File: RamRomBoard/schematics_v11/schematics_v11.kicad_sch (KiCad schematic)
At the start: 84 parts, among them J10 Micro_SD_Card_Det2, J3 VSEL, J5 Screw_Terminal_01x02, J6 USB_B_Micro, J7 STM32F401, J8 Dual LED Socket, J9 JTAG, SW1 033TBVSA, SW2 SW_Push, U1 74LVC125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

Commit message: first boards done, start of coding
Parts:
- added H5: Logo kicad, Symbol:KiCad-Logo2_6mm_SilkScreen, symbol Mechanical:MountingHole
- added H6: Logo Open Source Hardware, Symbol:OSHW-Logo2_7.3x6mm_SilkScreen, symbol Mechanical:MountingHole
- added H7: Logo 100%, my_own:Logo_100ProzentOffner_10x2.7mm, symbol Mechanical:MountingHole
- added JP1: CTRL, Jumper:SolderJumper-2_P1.3mm_Open_RoundedPad1.0x1.5mm, symbol Jumper:SolderJumper_2_Open
- added TP15: ., Connector_PinHeader_1.00mm:PinHeader_1x01_P1.00mm_Vertical, symbol Connector:TestPoint
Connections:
- net +3V3: no longer R5.1, R6.1
- net GND: now also R5.2, R6.2
- net at TP8.1, U4.5 (CTRL0): now also R5.1, JP1.1 (A); no longer R5.2
- net CNT renamed CPC
- net CTRL1: no longer names the net of TP9.1, U4.6 (CTRL1)
- net CTRL1: now also R6.1, JP1.2 (B); no longer J7.16 (Pin_16), R6.2
- net ~{CEDAT_EN} renamed ~{CERAMWR}
- net ~{MRAM_WR} renamed ~{MRAMWR}
- new net CTRL: J7.16 (Pin_16), TP15.1
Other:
- note added: "Graphics"
- note added: "~{MRAMWR} is Write Pulse from STM32."
- note removed: "~{MRAM_WR} is Write Pulse from STM32."
- moved on the sheet: R3, R4, R5, R6, TP8, TP9, U4

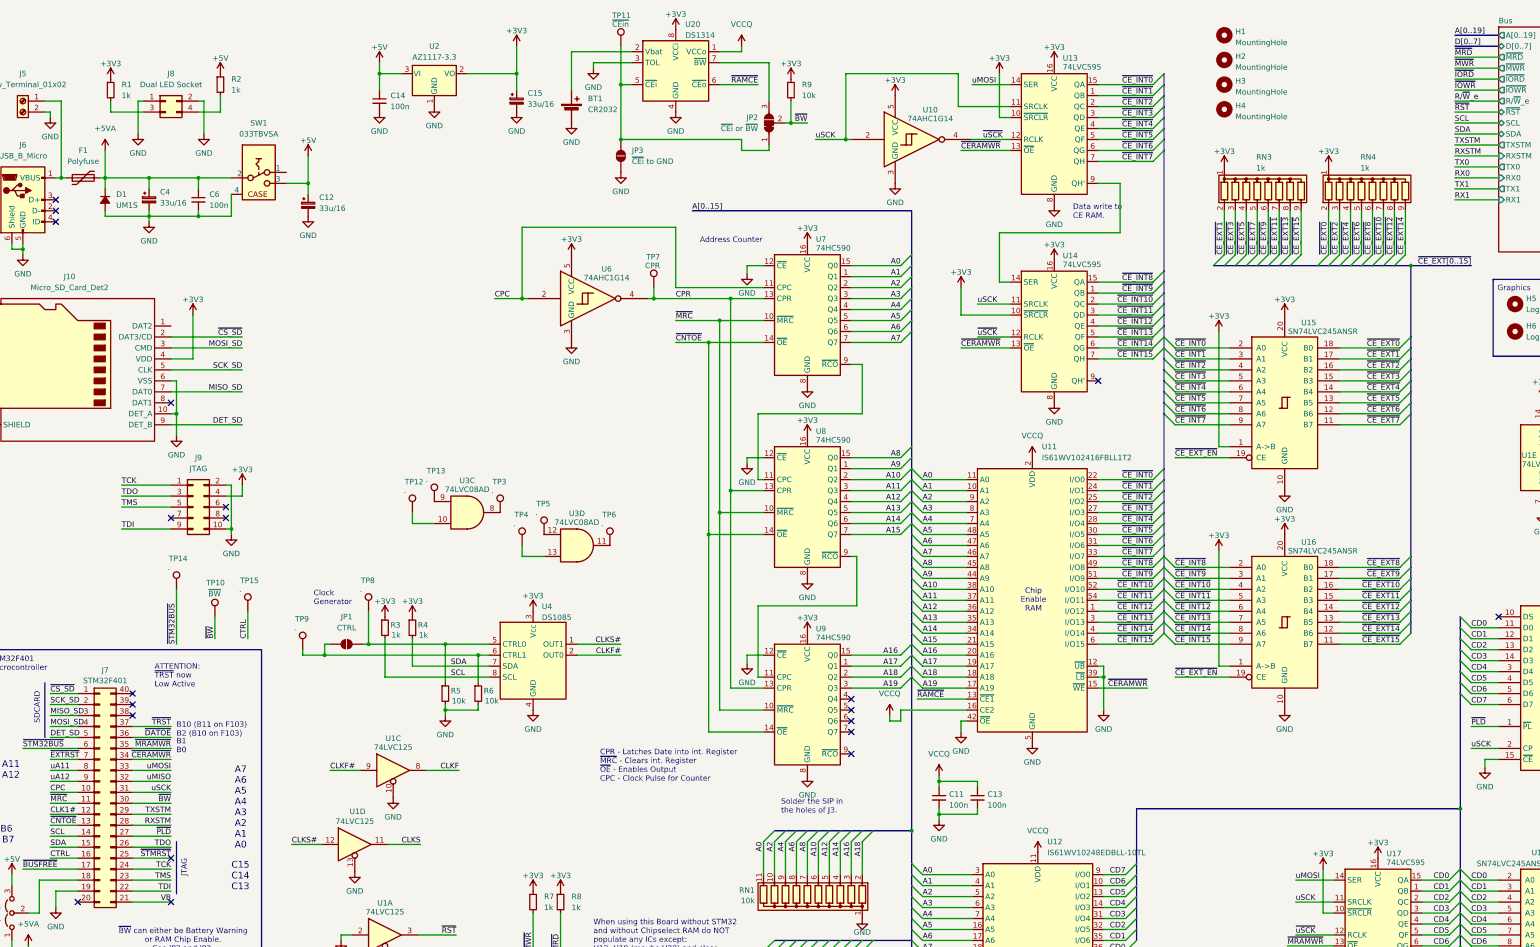
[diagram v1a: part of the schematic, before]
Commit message: new vhdl code
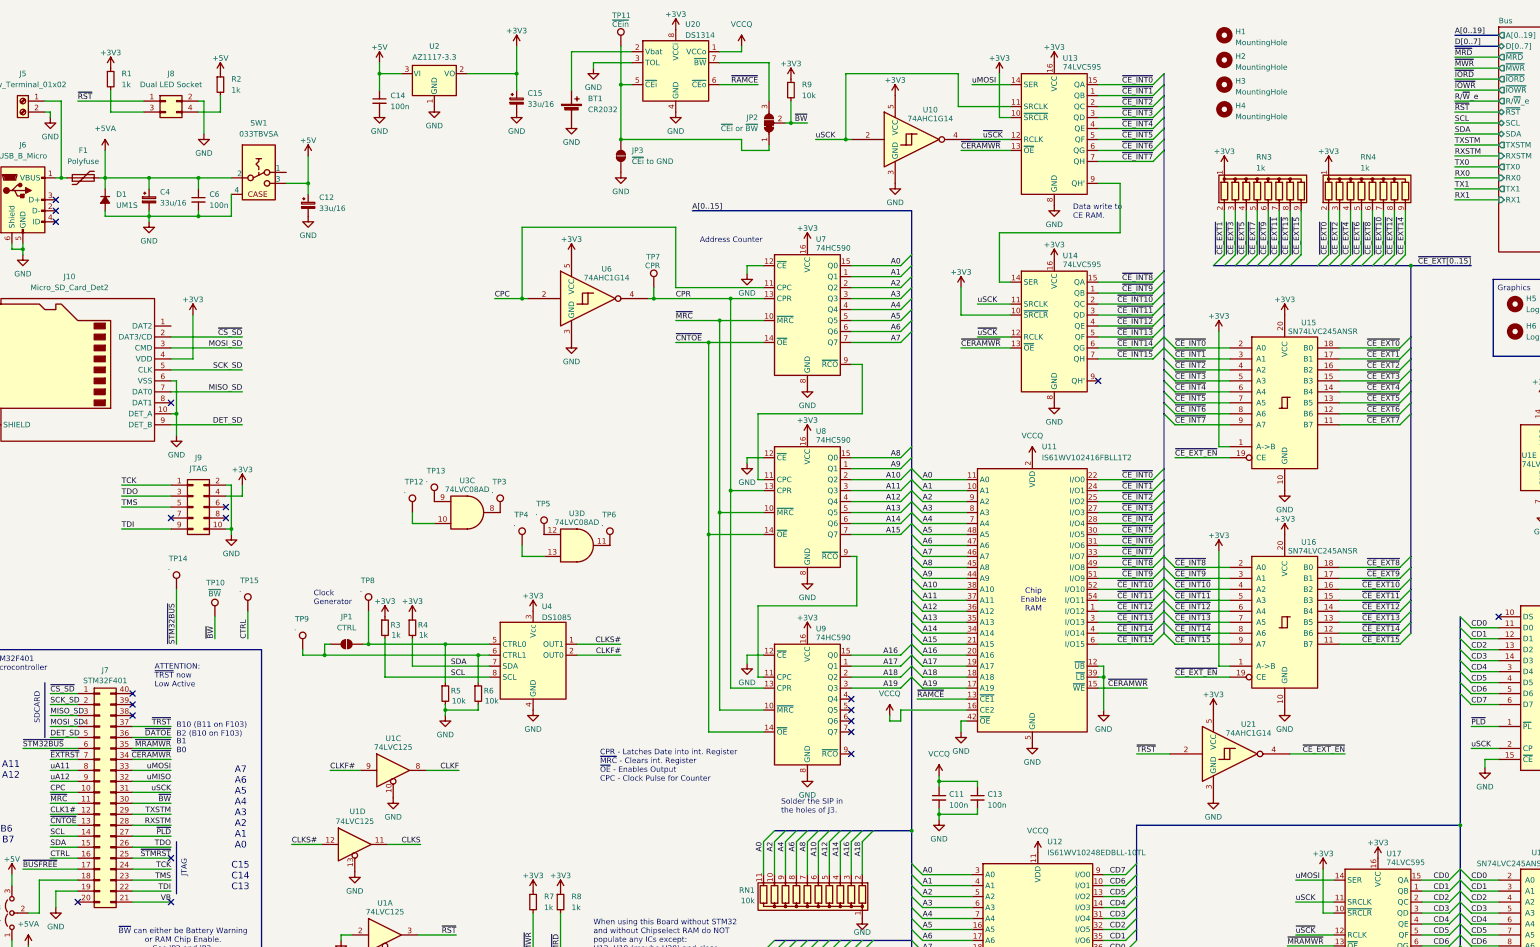
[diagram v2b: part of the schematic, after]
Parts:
- added U21: 74AHC1G14, Package_TO_SOT_SMD:SOT-23-5, symbol 74xGxx:74AHC1G14
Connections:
- net +3V3: now also U21.5 (VCC)
- net GND: now also U21.3 (GND); no longer J8.1 (Pin_1)
- net ~{CE_EXT_EN}: now also U21.4
- net ~{RST}: now also J8.1 (Pin_1)
- net ~{TRST}: now also U21.2
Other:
- moved on the sheet: R1

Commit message: graphic updates
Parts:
- added R11: 1k, Resistor_SMD:R_1206_3216Metric, symbol Device:R_Small
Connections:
- net +3V3: now also R11.1
- net R/~{W}_e: now also R11.2
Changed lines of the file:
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@@
 		(company "100% Offner")
 		(comment 1 "v1.0: Initial")
-		(comment 2 "v1.1: CTRL0 and CTRL1 ch. to Pulldown, second LED shows ~{RST}, U21 new")
+		(comment 2 "v1.1: CTRL0 and CTRL1 ch. to Pulldown, second LED shows ~{RST}, U21 new, R/W Pullup")
 	)
 	(junction
@@
 	(wire
 		(pts
+			(xy 137.16 220.98) (xy 137.16 229.87)
+		)
+		(stroke
+			(width 0)
+			(type default)
+		)
+	)
+	(wire
+		(pts
 			(xy 275.59 222.25) (xy 280.67 222.25)
 		)
@@
 		)
 	)
+	(label "R{slash}~{W}_e"
+		(at 137.16 229.87 90)
+		(fields_autoplaced yes)
+		(effects
+			(font
+				(size 1.27 1.27)
+			)
+			(justify left bottom)
+		)
+	)
 	(label "A12"
 		(at 212.09 204.47 270)
@@
 	(symbol
 		(lib_id "power:+3V3")
+		(at 137.16 215.9 0)
+		(unit 1)
+		(exclude_from_sim no)
+		(in_bom yes)
+		(on_board yes)
+		(dnp no)
+		(fields_autoplaced yes)
+		(property "Reference" "#PWR0133"
+			(at 137.16 219.71 0)
+			(effects
+				(font
+					(size 1.27 1.27)
+				)
+				(hide yes)
+			)
+		)
+		(property "Value" "+3V3"
+			(at 137.16 212.3242 0)
+			(effects
+				(font
+					(size 1.27 1.27)
+				)
+			)
+		)
+		(property "Footprint" ""
+			(at 137.16 215.9 0)
+			(effects
+				(font
+					(size 1.27 1.27)
+				)
+				(hide yes)
+			)
+		)
+		(property "Datasheet" ""
+			(at 137.16 215.9 0)
+			(effects
+				(font
+					(size 1.27 1.27)
+				)
+				(hide yes)
+			)
+		)
+		(property "Description" "Power symbol creates a global label with name \"+3V3\""
+			(at 137.16 215.9 0)
+			(effects
+				(font
+					(size 1.27 1.27)
+				)
+				(hide yes)
+			)
+		)
+		(pin "1"
+		)
+		(instances
+			(project "schematics_v11"
+				(path "/2eaa3998-c9cb-43b1-9b23-df656c8158b0"
+					(reference "#PWR0133")
+					(unit 1)
+				)
+			)
+		)
+	)
+	(symbol
+		(lib_id "power:+3V3")
 		(at 109.22 152.4 0)
 		(unit 1)
@@
 	)
 	(symbol
+		(lib_id "Device:R_Small")
+		(at 137.16 218.44 0)
+		(unit 1)
+		(exclude_from_sim no)
+		(in_bom yes)
+		(on_board yes)
+		(dnp no)
+		(property "Reference" "R11"
+			(at 138.43 217.805 0)
+			(effects
+				(font
+					(size 1.27 1.27)
+				)
+				(justify left)
+			)
+		)
+		(property "Value" "1k"
+			(at 138.6586 220.1422 0)
+			(effects
+				(font
+					(size 1.27 1.27)
+				)
+				(justify left)
+			)
+		)
+		(property "Footprint" "Resistor_SMD:R_1206_3216Metric"
+			(at 137.16 218.44 0)
+			(effects
+				(font
+					(size 1.27 1.27)
+				)
+				(hide yes)
+			)
+		)
+		(property "Datasheet" "~"
+			(at 137.16 218.44 0)
+			(effects
+				(font
+					(size 1.27 1.27)
+				)
+				(hide yes)
+			)
+		)
+		(property "Description" "Resistor, small symbol"
+			(at 137.16 218.44 0)
+			(effects
+				(font
+					(size 1.27 1.27)
+				)
+				(hide yes)
+			)
+		)
+		(pin "1"
+		)
+		(pin "2"
+		)
+		(instances
+			(project "schematics_v11"
+				(path "/2eaa3998-c9cb-43b1-9b23-df656c8158b0"
+					(reference "R11")
+					(unit 1)
+				)
+			)
+		)
+	)
+	(symbol
 		(lib_id "Mechanical:MountingHole")
 		(at 303.53 17.78 0)
@@
 	(symbol
 		(lib_id "Graphic:Logo_Open_Hardware_Small")
-		(at 398.78 261.62 0)
+		(at 401.32 247.65 0)
 		(unit 1)
 		(exclude_from_sim yes)
@@
 		(fields_autoplaced yes)
 		(property "Reference" "#SYM1"
-			(at 398.78 254.635 0)
+			(at 401.32 240.665 0)
 			(effects
 				(font
@@
 		)
 		(property "Value" "Logo_Open_Hardware_Small"
-			(at 398.78 267.335 0)
+			(at 401.32 253.365 0)
 			(effects
 				(font
@@
 		)
 		(property "Footprint" ""
-			(at 398.78 261.62 0)
+			(at 401.32 247.65 0)
 			(effects
 				(font
@@
 		)
 		(property "Datasheet" "~"
-			(at 398.78 261.62 0)
+			(at 401.32 247.65 0)
 			(effects
 				(font
@@
 		)
 		(property "Description" "Open Hardware logo, small"
-			(at 398.78 261.62 0)
+			(at 401.32 247.65 0)
 			(effects
 				(font
